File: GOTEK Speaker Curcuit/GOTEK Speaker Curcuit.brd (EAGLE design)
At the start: 22.8 x 22.5 mm, 4 parts, among them T1 2N3904

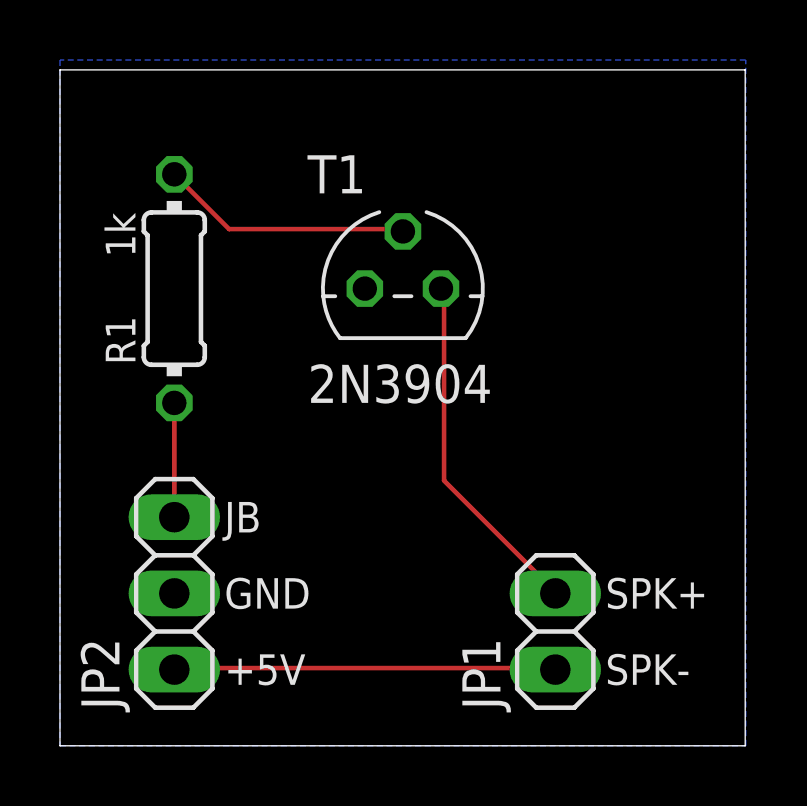
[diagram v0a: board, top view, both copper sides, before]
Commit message: Modified GOTEK board to add 4 pin header for speaker
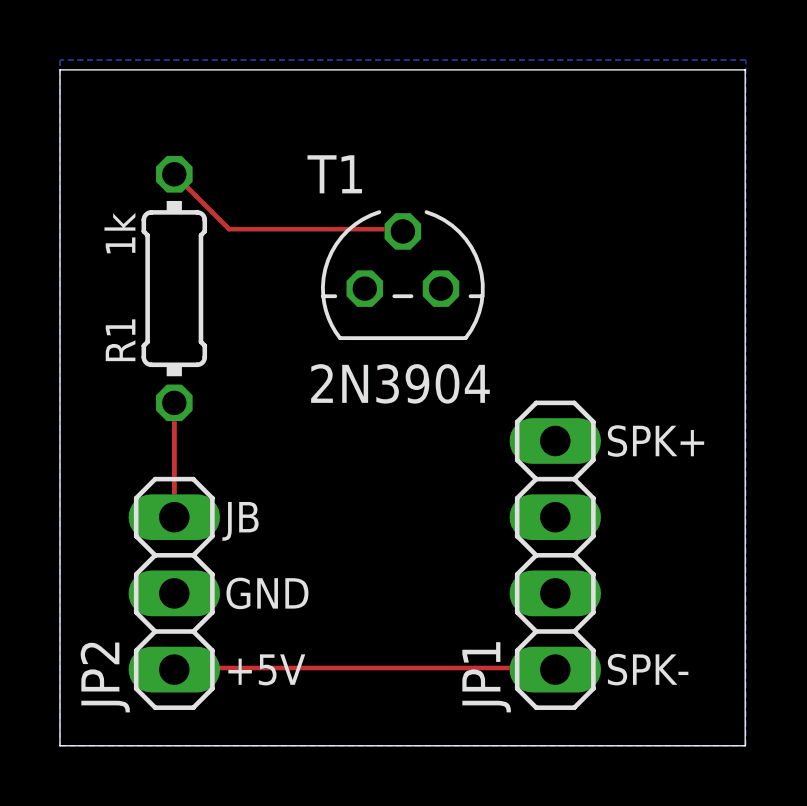
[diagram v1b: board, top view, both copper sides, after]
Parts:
- JP1: value SPEAKER -> (none); device pinhead:1X02 -> pinhead:1X04
- moved JP1 2.54 mm to (16.5, 6.35)
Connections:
- net SPK-: now also JP1.4; no longer JP1.2
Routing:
- net SPK-: track 11.8 -> 0.00 mm
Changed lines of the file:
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@@
 <text x="5.08" y="5.08" size="1.016" layer="21" align="center-left"> GND</text>
 <text x="5.08" y="7.62" size="1.016" layer="21" align="center-left"> JB</text>
-<text x="17.78" y="5.08" size="1.016" layer="21" align="center-left"> SPK+</text>
+<text x="17.78" y="10.16" size="1.016" layer="21" align="center-left"> SPK+</text>
 <text x="17.78" y="2.54" size="1.016" layer="21" align="center-left"> SPK-</text>
 <text x="11.43" y="11.43" size="1.016" layer="22" rot="MR180" align="center">ACTVIE BUZZER CIRCUIT
@@
 </autorouter>
 <elements>
-<element name="JP1" library="pinhead" library_urn="urn:adsk.eagle:library:325" package="1X02" package3d_urn="urn:adsk.eagle:package:22435/2" value="SPEAKER" x="16.51" y="3.81" smashed="yes" rot="R90">
-<attribute name="NAME" x="14.6812" y="1.1938" size="1.27" layer="25" ratio="10" rot="R90"/>
-<attribute name="POPULARITY" value="98" x="25.4" y="20.32" size="1.778" layer="27" rot="R90" display="off"/>
-<attribute name="VALUE" x="19.685" y="1.27" size="1.27" layer="27" rot="R90" display="off"/>
-</element>
 <element name="JP2" library="pinhead" library_urn="urn:adsk.eagle:library:325" package="1X03" package3d_urn="urn:adsk.eagle:package:22458/2" value="JP2" x="3.81" y="5.08" smashed="yes" rot="R90">
 <attribute name="NAME" x="1.9812" y="1.1938" size="1.27" layer="25" ratio="10" rot="R90"/>
@@
 <attribute name="VALUE" x="8.255" y="11.43" size="1.27" layer="21" ratio="10"/>
 </element>
+<element name="JP1" library="pinhead" library_urn="urn:adsk.eagle:library:325" package="1X04" package3d_urn="urn:adsk.eagle:package:22407/2" value="" x="16.51" y="6.35" smashed="yes" rot="R90">
+<attribute name="NAME" x="14.6812" y="1.1938" size="1.27" layer="25" ratio="10" rot="R90"/>
+<attribute name="POPULARITY" value="91" x="16.51" y="6.35" size="1.778" layer="27" rot="R90" display="off"/>
+<attribute name="VALUE" x="19.685" y="1.27" size="1.27" layer="27" rot="R90"/>
+</element>
 </elements>
 <signals>
 <signal name="+5V">
 <contactref element="JP2" pad="1"/>
-<contactref element="JP1" pad="1"/>
 <wire x1="16.4592" y1="2.5908" x2="3.81" y2="2.5908" width="0.1524" layer="1"/>
 <wire x1="3.81" y1="2.5908" x2="3.81" y2="2.54" width="0.1524" layer="1"/>
-<wire x1="16.4592" y1="2.5908" x2="16.51" y2="2.54" width="0.1524" layer="1"/>
+<contactref element="JP1" pad="1"/>
+<wire x1="16.51" y1="2.54" x2="3.81" y2="2.54" width="0" layer="19" extent="1-1"/>
 </signal>
 <signal name="GND">
@@
 </signal>
 <signal name="SPK-">
-<contactref element="JP1" pad="2"/>
+<contactref element="JP1" pad="4"/>
 <contactref element="T1" pad="1"/>
-<wire x1="12.8016" y1="8.8392" x2="12.8016" y2="15.24" width="0.1524" layer="1"/>
-<wire x1="16.4592" y1="5.1816" x2="12.8016" y2="8.8392" width="0.1524" layer="1"/>
-<wire x1="12.8016" y1="15.24" x2="12.7" y2="15.24" width="0.1524" layer="1"/>
-<wire x1="16.4592" y1="5.1816" x2="16.51" y2="5.08" width="0.1524" layer="1"/>
+<wire x1="16.51" y1="10.16" x2="12.7" y2="15.24" width="0" layer="19" extent="1-1"/>
 </signal>
 </signals>
